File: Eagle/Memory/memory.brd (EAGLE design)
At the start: 100 x 100 mm, 20 parts

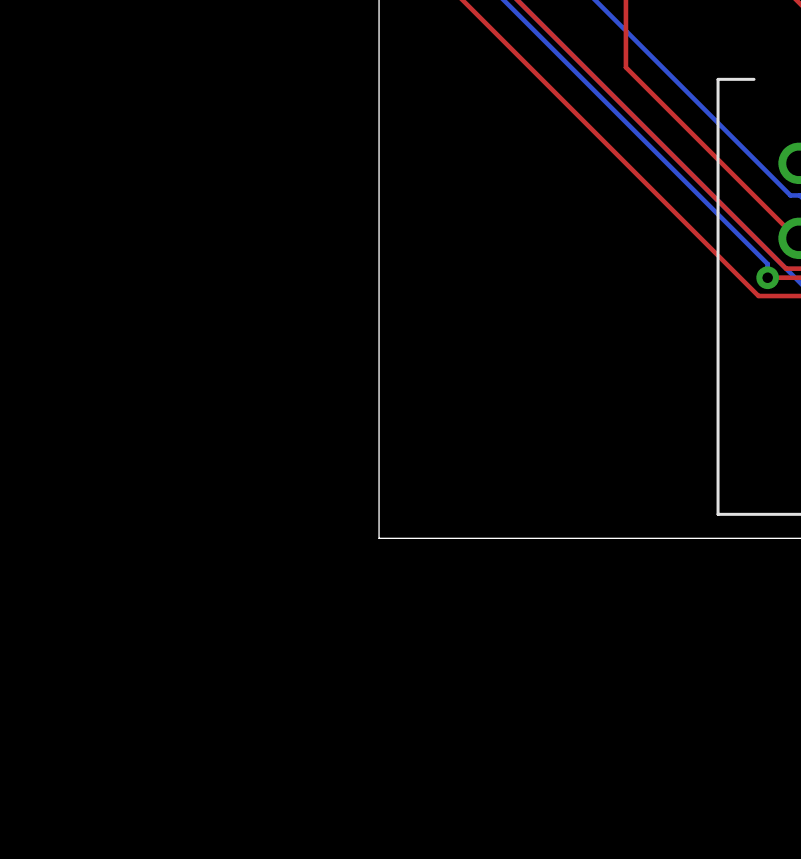
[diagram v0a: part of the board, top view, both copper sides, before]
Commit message: added parts needed to finish boards
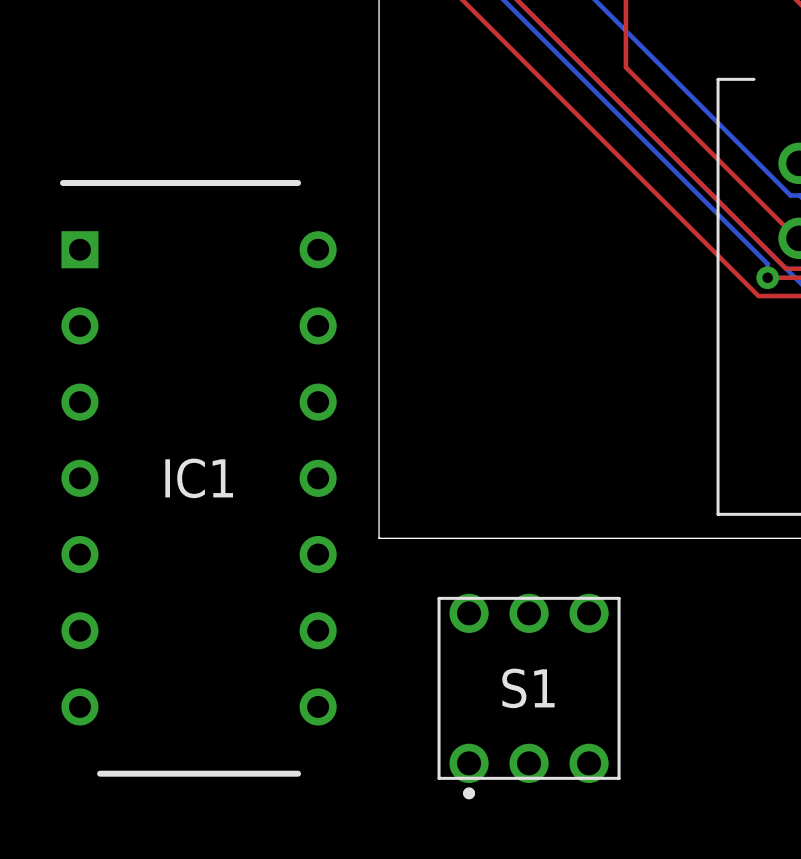
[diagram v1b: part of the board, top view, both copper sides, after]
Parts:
- added IC1: SN74HC02N, SamacSys_Parts:DIP794W53P254L1930H508Q14N
- added S1: MHPS2273N, SamacSys_Parts:MHPS2273N
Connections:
- net GND: now also S1.A3
- net N$2: now also S1.A2
- net VCC: now also S1.A1
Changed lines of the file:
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@@
 <attribute name="VALUE" x="91" y="85" size="1.27" layer="27" align="center"/>
+</element>
+<element name="S1" library="SamacSys_Parts" package="MHPS2273N" value="MHPS2273N" x="5" y="-5" smashed="yes">
+<attribute name="DESCRIPTION" value="Pushbutton Switches Momentary key DP" x="5" y="-5" size="1.778" layer="27" display="off"/>
+<attribute name="HEIGHT" value="13.5mm" x="5" y="-5" size="1.778" layer="27" display="off"/>
+<attribute name="MANUFACTURER_NAME" value="Apem" x="5" y="-5" size="1.778" layer="27" display="off"/>
+<attribute name="MANUFACTURER_PART_NUMBER" value="MHPS2273N" x="5" y="-5" size="1.778" layer="27" display="off"/>
+<attribute name="MOUSER_PART_NUMBER" value="642-MHPS2273N" x="5" y="-5" size="1.778" layer="27" display="off"/>
+<attribute name="MOUSER_PRICE-STOCK" value="https://www.mouser.com/Search/Refine.aspx?Keyword=642-MHPS2273N" x="5" y="-5" size="1.778" layer="27" display="off"/>
+<attribute name="NAME" x="5" y="-5" size="1.27" layer="25" align="center"/>
+<attribute name="VALUE" x="5" y="-5" size="1.27" layer="27" align="center"/>
+</element>
+<element name="IC1" library="SamacSys_Parts" package="DIP794W53P254L1930H508Q14N" value="SN74HC02N" x="-6" y="2" smashed="yes">
+<attribute name="DESCRIPTION" value="Quad 2i/p NOR gate,SN74HC02N DIP14 25pcs" x="-6" y="2" size="1.778" layer="27" display="off"/>
+<attribute name="HEIGHT" value="5.08mm" x="-6" y="2" size="1.778" layer="27" display="off"/>
+<attribute name="MANUFACTURER_NAME" value="Texas Instruments" x="-6" y="2" size="1.778" layer="27" display="off"/>
+<attribute name="MANUFACTURER_PART_NUMBER" value="SN74HC02N" x="-6" y="2" size="1.778" layer="27" display="off"/>
+<attribute name="MOUSER_PART_NUMBER" value="595-SN74HC02N" x="-6" y="2" size="1.778" layer="27" display="off"/>
+<attribute name="MOUSER_PRICE-STOCK" value="https://www.mouser.com/Search/Refine.aspx?Keyword=595-SN74HC02N" x="-6" y="2" size="1.778" layer="27" display="off"/>
+<attribute name="NAME" x="-6" y="2" size="1.27" layer="25" align="center"/>
+<attribute name="VALUE" x="-6" y="2" size="1.27" layer="27" align="center"/>
 </element>
 </elements>
@@
 <via x="76.0476" y="40.5384" extent="1-16" drill="0.35"/>
 <via x="39.1668" y="72.0852" extent="1-16" drill="0.35"/>
+<contactref element="S1" pad="A1"/>
+<wire x1="3" y1="-7.5" x2="37.973" y2="6.651" width="0" layer="19" extent="1-1"/>
 </signal>
 <signal name="GND">
@@
 <via x="49.0728" y="89.7636" extent="1-16" drill="0.35"/>
 <via x="60.5028" y="36.7284" extent="1-16" drill="0.35"/>
+<contactref element="S1" pad="A3"/>
+<wire x1="7" y1="-7.5" x2="5.03" y2="21.38" width="0" layer="19" extent="1-1"/>
 </signal>
 <signal name="DIP0">
@@
 <signal name="N$2">
 <contactref element="BOARD_WRITE" pad="3"/>
+<contactref element="S1" pad="A2"/>
+<wire x1="5" y1="-7.5" x2="10.19" y2="69.03" width="0" layer="19" extent="1-1"/>
 </signal>
 </signals>

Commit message: finished most boards
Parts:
- removed IC1: SN74HC02N, SamacSys_Parts:DIP794W53P254L1930H508Q14N
- added C1, C2, C3, C4: (no value), rcl:C025-024X044
- added LED0, LED1, LED10, LED11, LED12, LED13, LED14, LED15, LED2, LED3, LED4, LED5, LED6, LED7, LED8, LED9: RED, led:LED3MM
- added R0, R1, R10, R11, R12, R13, R14, R15, R2, R3, R4, R5, R6, R7, R8, R9: 220, rcl:0204/7
- added U$1, U$2, U$3, U$4: (no value), holes:2,8
- moved S1 92.3 mm to (85.0, 41.0)
- moved MAR 35.5 mm to (61.0, 4.00)
- moved BUS/DIP_8-11 31.9 mm to (14.9, 56.6)
- moved BUS/DIP_0-3 31.1 mm to (82.2, 56.6)
- moved DIP_0-7 29.7 mm to (62.7, 39.3), flipped to the bottom, turned to 270 degrees
- moved DIP_8-15 29.6 mm to (39.1, 39.3), flipped to the bottom, turned to 270 degrees
- moved BUS/DIP_4-7 26.8 mm to (60.5, 56.6)
- moved AND_GATE 18.7 mm to (14.0, 11.0), turned to 180 degrees
- moved BUS/DIP_12-15 17.0 mm to (6.44, 32.3)
- moved RAM_OUT_0-7 10.8 mm to (85.0, 73.0), turned to 90 degrees
- moved ARD/BRD_0-3 10.0 mm to (71.5, 56.3)
- moved MEMORY_8-15 10.0 mm to (30.9, 88.6)
- moved BUS 8.25 mm to (96.8, 63.5)
- moved ARDUINO 8.06 mm to (2.18, 47.0)
- moved MEMORY_0-7 8.00 mm to (71.0, 88.4)
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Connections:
- new net N$10: LED8.A, R8.1
- new net N$11: LED9.A, R9.1
- new net N$12: LED10.A, R10.1
- new net N$13: LED11.A, R11.1
- new net N$14: LED12.A, R12.1
- new net N$15: LED13.A, R13.1
- new net N$16: LED14.A, R14.1
- new net N$17: LED15.A, R15.1
- new net N$18: LED0.A, R0.1
- new net N$4: LED2.A, R2.1
- new net N$5: LED3.A, R3.1
- new net N$6: LED4.A, R4.1
- new net N$7: LED5.A, R5.1
- new net N$8: LED6.A, R6.1
- new net N$9: LED7.A, R7.1
- net GND: now also ARDUINO_WRITE.4, C1.1, C2.1, C3.1, C4.1, MEMORY_0-7.27, MEMORY_8-15.27
- net N$1: now also LED1.A, R1.1; no longer ARDUINO_WRITE.4, MEMORY_0-7.27, MEMORY_8-15.27
- net RAM0: now also R0.2
- net RAM1: now also R1.2
- net RAM10: now also R10.2
- net RAM11: now also R11.2
- net RAM12: now also R12.2
- net RAM13: now also R13.2
- net RAM14: now also R14.2
- net RAM15: now also R15.2
- net RAM2: now also R2.2
- net RAM3: now also R3.2
- net RAM4: now also R4.2
- net RAM5: now also R5.2
- net RAM6: now also R6.2
- net RAM7: now also R7.2
- net RAM8: now also R8.2
- net RAM9: now also R9.2
- net VCC: now also C1.2, C2.2, C3.2, C4.2
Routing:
- net N$2: track 0.00 -> 116.4 mm, vias 0 -> 8
- net VCC: track 510.0 -> 398.9 mm, vias 4 -> 7
- net B12: track 176.5 -> 267.1 mm
- net B0: track 106.1 -> 35.3 mm, vias 1 -> 0
- net RAM0: track 53.4 -> 122.2 mm, vias 2 -> 3
- net B2: track 106.1 -> 38.5 mm, vias 0 -> 1
- net RAM7: track 89.6 -> 156.9 mm
- net RAM3: track 53.2 -> 118.8 mm, vias 0 -> 2
- net ARD1: track 82.1 -> 145.5 mm, vias 1 -> 4
- net N$1: track 73.3 -> 10.3 mm, vias 2 -> 0
- net A1: track 158.9 -> 221.1 mm, vias 1 -> 4
- net PRGM: track 166.6 -> 227.1 mm, vias 4 -> 11
- net RAM15: track 113.0 -> 171.2 mm, vias 6 -> 9
- net B15: track 135.8 -> 193.8 mm, vias 4 -> 5
- net RAM5: track 86.7 -> 143.6 mm, vias 2 -> 5
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
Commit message: added gerber files for each board
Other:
- board text added: "MARIE PC Memory Architecture design by: Dr. Linda Null Hardware implementation by: Richard Bowser"
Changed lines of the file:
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@@
 <wire x1="100" y1="100" x2="0" y2="100" width="0" layer="20"/>
 <wire x1="0" y1="100" x2="0" y2="0" width="0" layer="20"/>
+<text x="63" y="84" size="1.778" layer="26" rot="MR0">MARIE PC
+Memory
+Architecture design by: Dr. Linda Null
+Hardware implementation by: Richard Bowser</text>
 </plain>
 <attributes>
@@
 </drawing>
 <compatibility>
+<note version="6.3" minversion="6.2.2" severity="warning">
+Since Version 6.2.2 text objects can contain more than one line,
+which will not be processed correctly with this version.
+</note>
 <note version="8.2" severity="warning">
 Since Version 8.2, EAGLE supports online libraries. The ids

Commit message: added gerber files for ordering boards
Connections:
- net GND: now also LED0.K, LED1.K, LED10.K, LED11.K, LED12.K, LED13.K, LED14.K, LED15.K, LED2.K, LED3.K, LED4.K, LED5.K, LED6.K, LED7.K, LED8.K, LED9.K
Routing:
- net B12: track 267.1 -> 192.4 mm, vias 2 -> 8
- net A1: track 221.1 -> 150.9 mm
- net GND: track 568.4 -> 637.2 mm, vias 7 -> 12
- net A4: track 141.4 -> 193.5 mm, vias 6 -> 10
- net B8: track 118.4 -> 162.8 mm
- net RAM0: track 122.2 -> 79.3 mm, vias 3 -> 6
- net ARD0: track 123.5 -> 80.7 mm
- net B10: track 134.9 -> 174.5 mm, vias 10 -> 9
- net B9: track 134.1 -> 173.2 mm, vias 7 -> 12
- net B14: track 193.4 -> 225.6 mm, vias 7 -> 13
- net B7: track 80.1 -> 110.5 mm, vias 3 -> 4
- net B5: track 111.0 -> 81.6 mm, vias 6 -> 7
- net RAM2: track 105.1 -> 77.0 mm
- net N$2: track 116.4 -> 140.8 mm
- net A6: track 176.6 -> 154.3 mm, vias 4 -> 5
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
